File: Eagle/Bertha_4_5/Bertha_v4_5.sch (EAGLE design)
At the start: 132 parts, among them CON1 JACK_DC_BARREL, CON2 JACK_DC_BARREL, IC1 MCP1703DB, IC4 DRV8811, J1 RJ12RIGHTANGLE-I2C, J2 RJ12RIGHTANGLE-I2C, Q5 BSP75, Q6 BSP75, U1 HX711, U100 RN2483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

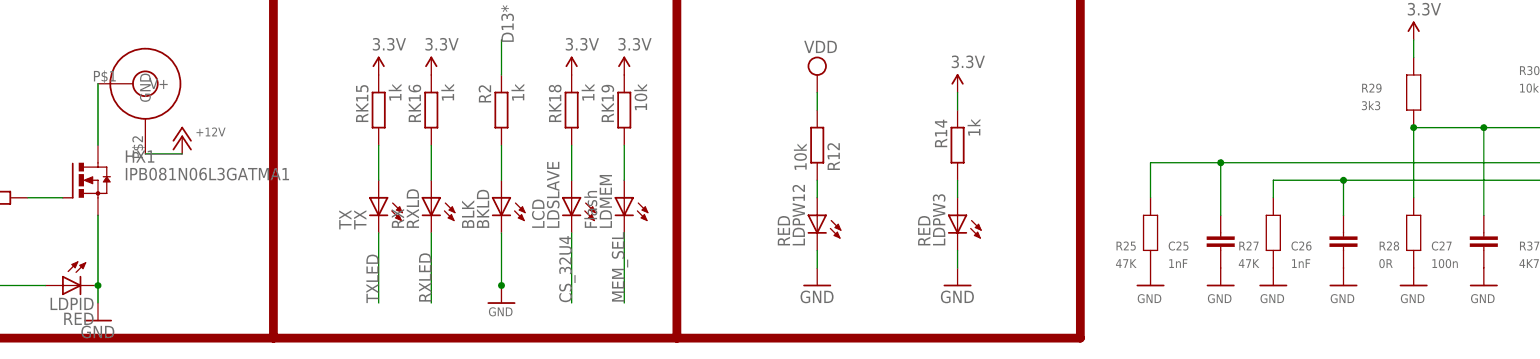
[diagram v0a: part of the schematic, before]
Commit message: correted PID diode, 4.5 finished, closes #72, ref #47
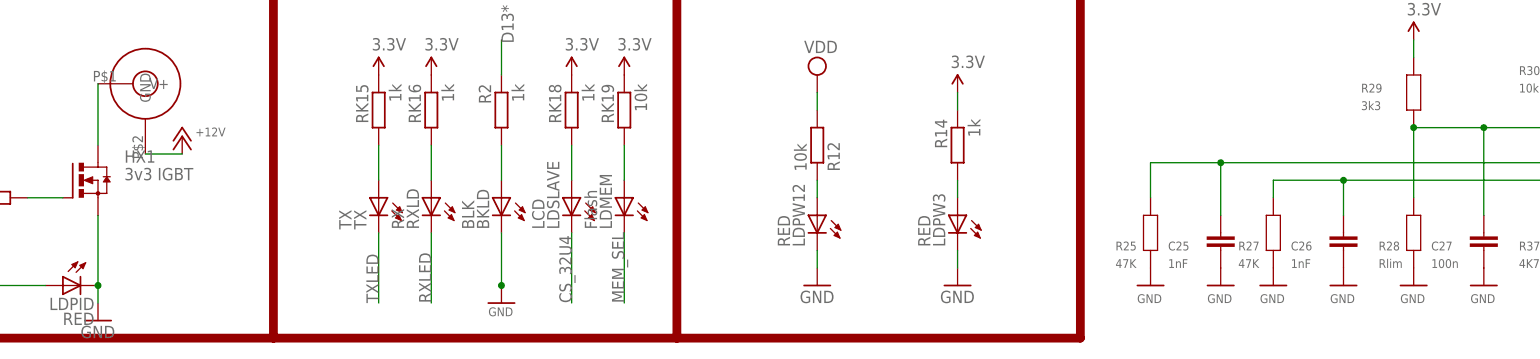
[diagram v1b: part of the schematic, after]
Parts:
- HX1: value IPB081N06L3GATMA1 -> 3v3 IGBT
- R28: value 0R -> Rlim
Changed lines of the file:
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@@
 <?xml version="1.0" encoding="utf-8"?>
 <!DOCTYPE eagle SYSTEM "eagle.dtd">
-<eagle version="7.7.0">
+<eagle version="6.5.0">
 <drawing>
 <settings>
@@
 <part name="GND8" library="supply1" deviceset="GND" device=""/>
 <part name="GND27" library="supply1" deviceset="GND" device=""/>
-<part name="HX1" library="transistor-power" deviceset="IRF3704" device="S" value="IPB081N06L3GATMA1"/>
+<part name="HX1" library="transistor-power" deviceset="IRF3704" device="S" value="3v3 IGBT"/>
 <part name="R11" library="rcl" deviceset="R-EU_" device="R0805" value="1K"/>
 <part name="P+2" library="supply1" deviceset="+12V" device=""/>
@@
 <part name="R27" library="freetronics-master-v1" deviceset="RESISTOR" device="0805" value="47K"/>
 <part name="C26" library="freetronics-master-v1" deviceset="CAP" device="0805" value="1nF"/>
-<part name="R28" library="freetronics-master-v1" deviceset="RESISTOR" device="0805" value="0R"/>
+<part name="R28" library="freetronics-master-v1" deviceset="RESISTOR" device="0805" value="Rlim"/>
 <part name="C27" library="freetronics-master-v1" deviceset="CAP" device="0805" value="100n"/>
 <part name="R29" library="freetronics-master-v1" deviceset="RESISTOR" device="0805" value="3k3"/>

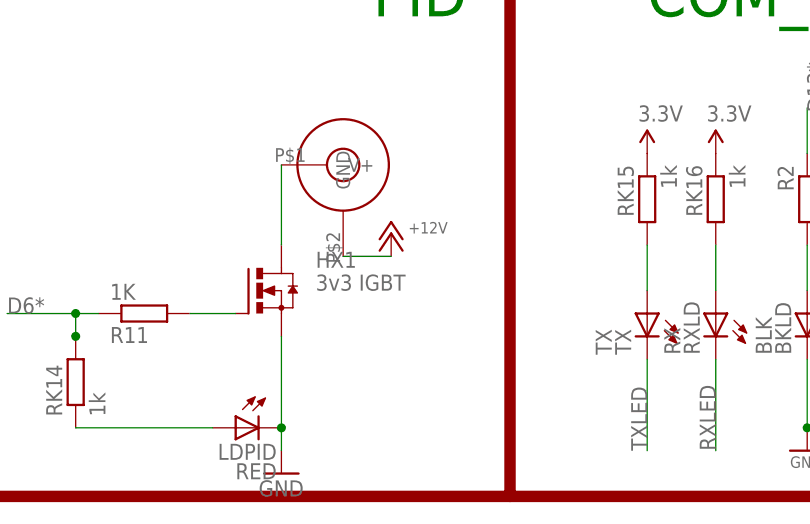
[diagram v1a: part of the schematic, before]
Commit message: corrected powerFET labelling
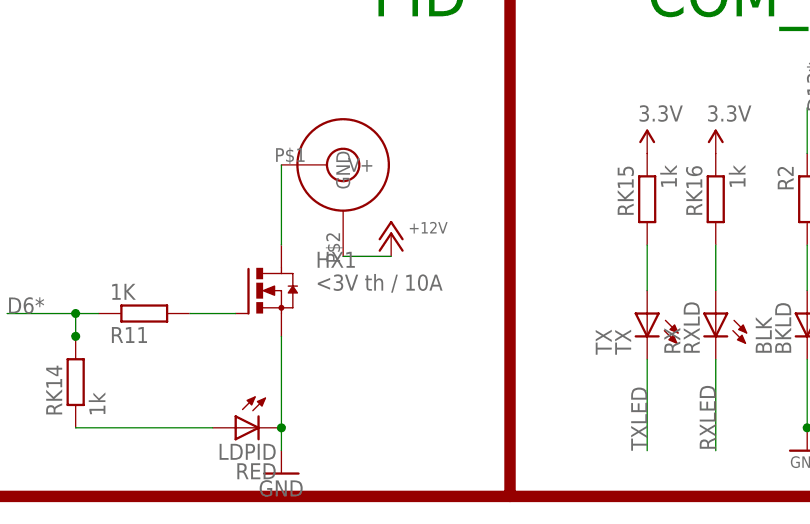
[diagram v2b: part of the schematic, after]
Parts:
- HX1: value 3v3 IGBT -> <3V th / 10A
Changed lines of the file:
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@@
 <part name="GND8" library="supply1" deviceset="GND" device=""/>
 <part name="GND27" library="supply1" deviceset="GND" device=""/>
-<part name="HX1" library="transistor-power" deviceset="IRF3704" device="S" value="3v3 IGBT"/>
+<part name="HX1" library="transistor-power" deviceset="IRF3704" device="S" value="&lt;3V th / 10A"/>
 <part name="R11" library="rcl" deviceset="R-EU_" device="R0805" value="1K"/>
 <part name="P+2" library="supply1" deviceset="+12V" device=""/>

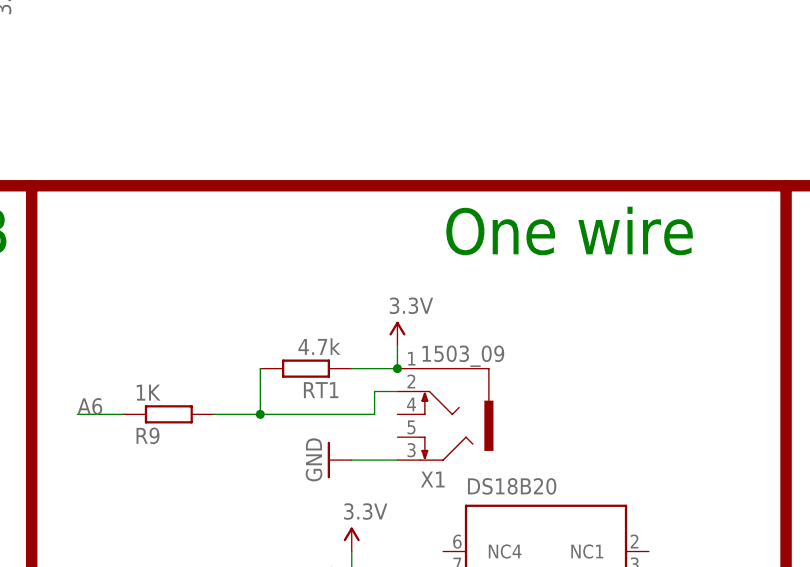
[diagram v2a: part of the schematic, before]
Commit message: added protection resistor, closes #74
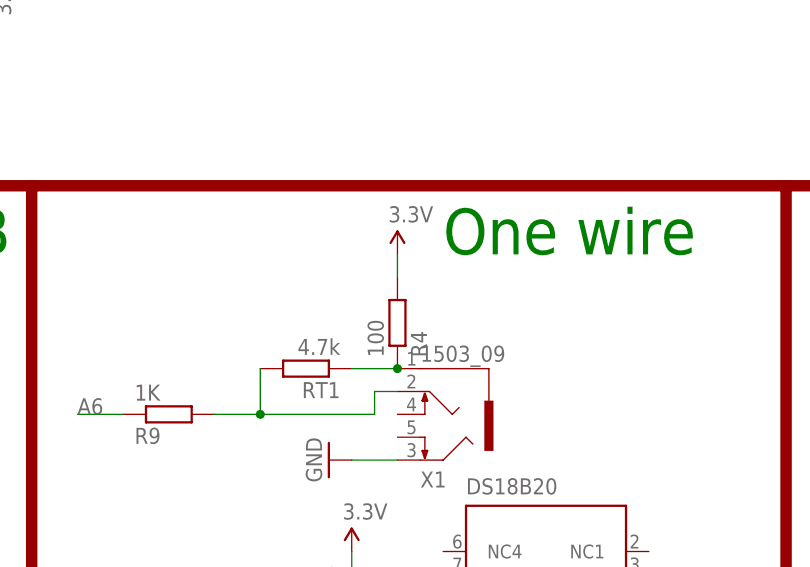
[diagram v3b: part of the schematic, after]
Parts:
- added R4: 100, rcl:R-EU_R0805
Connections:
- new net N$14: R4.1, RT1.1, X1.1
- net 3.3V: now also R4.2; no longer RT1.1, X1.1
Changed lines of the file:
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@@
 <part name="P+62" library="SparkFun" deviceset="3.3V" device=""/>
 <part name="JP3" library="jumper" deviceset="JP4E" device=""/>
+<part name="R4" library="rcl" deviceset="R-EU_" device="R0805" value="100"/>
 </parts>
 <sheets>
@@
 <instance part="P+35" gate="G$1" x="30.48" y="116.84"/>
 <instance part="P+36" gate="G$1" x="274.32" y="27.94"/>
-<instance part="P+37" gate="G$1" x="279.4" y="50.8"/>
+<instance part="P+37" gate="G$1" x="279.4" y="60.96"/>
 <instance part="P+39" gate="G$1" x="401.32" y="45.72"/>
 <instance part="P+40" gate="G$1" x="408.94" y="45.72"/>
@@
 <instance part="P+62" gate="G$1" x="693.42" y="53.34"/>
 <instance part="JP3" gate="G$1" x="673.1" y="48.26" rot="R270"/>
+<instance part="R4" gate="G$1" x="279.4" y="53.34" rot="MR90"/>
 </instances>
 <busses>
@@
 </segment>
 <segment>
-<pinref part="RT1" gate="G$1" pin="1"/>
-<pinref part="P+37" gate="G$1" pin="3.3V"/>
-<wire x1="279.4" y1="50.8" x2="279.4" y2="48.26" width="0.1524" layer="91"/>
-<pinref part="X1" gate="G$1" pin="1"/>
-<junction x="279.4" y="48.26"/>
-<wire x1="279.4" y1="48.26" x2="274.32" y2="48.26" width="0.1524" layer="91"/>
-</segment>
-<segment>
 <pinref part="RK15" gate="G$1" pin="1"/>
 <pinref part="P+39" gate="G$1" pin="3.3V"/>
@@
 <pinref part="P+62" gate="G$1" pin="3.3V"/>
 </segment>
+<segment>
+<pinref part="R4" gate="G$1" pin="2"/>
+<pinref part="P+37" gate="G$1" pin="3.3V"/>
+<wire x1="279.4" y1="60.96" x2="279.4" y2="58.42" width="0.1524" layer="91"/>
+</segment>
 </net>
 <net name="SDA" class="0">
@@
 </segment>
 </net>
+<net name="N$14" class="1">
+<segment>
+<pinref part="RT1" gate="G$1" pin="1"/>
+<pinref part="X1" gate="G$1" pin="1"/>
+<wire x1="279.4" y1="48.26" x2="274.32" y2="48.26" width="0.1524" layer="91"/>
+<pinref part="R4" gate="G$1" pin="1"/>
+<junction x="279.4" y="48.26"/>
+</segment>
+</net>

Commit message: added high side power switch with 5.6V zener on V4.5, drafted hack modif on 4.4, To be tested
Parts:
- added BJ2: MMBT4403, SparkFun-DiscreteSemi:TRANSISTOR_PNPMMBT4403
- added D6: 5.6V ZNR, diode:ZENER-DIODESOD80C
- added RK17, RK20: 1k, rcl:R-EU_R0805
- added T1: 2n7002, zetex:NMOSSOT23
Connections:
- new net N$16: BJ2.C, R11.1, RK14.2
- new net N$19: BJ2.E, D6.C, RK17.1
- new net N$31: BJ2.B, RK20.1
- new net N$32: RK20.2, T1.D
- net +12V: now also RK17.2
- net D6*: now also T1.G; no longer R11.1, RK14.2
- net GND: now also D6.A, T1.S
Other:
- moved on the sheet: CU7, CU8, IC1

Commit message: pretty sch for 4.5
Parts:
- RK14: value 1k -> 10k
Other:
- moved on the sheet: 12V, 32U4, 3V3, C10, C11, C12, C13, C25, C26, C27, C28, C29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

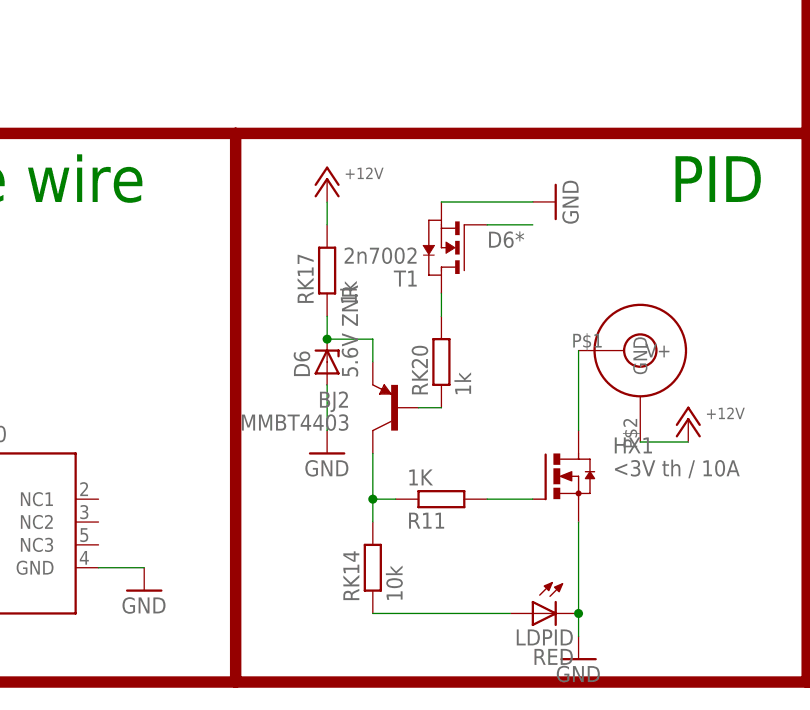
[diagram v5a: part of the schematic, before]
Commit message: JTAG on top
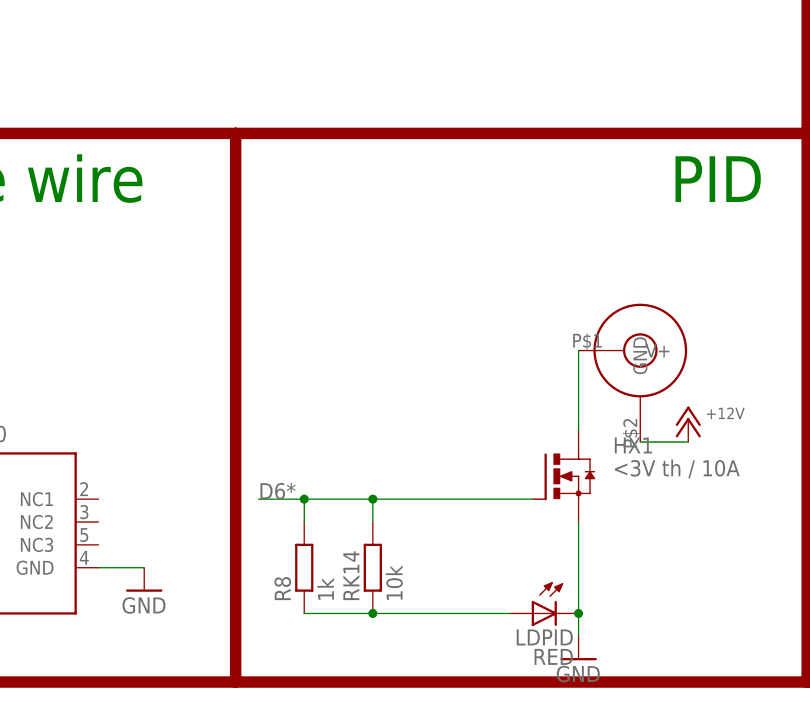
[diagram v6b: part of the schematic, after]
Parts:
- removed BJ2: MMBT4403, SparkFun-DiscreteSemi:TRANSISTOR_PNPMMBT4403
- removed D6: 5.6V ZNR, diode:ZENER-DIODESOD80C
- removed R11: 1K, rcl:R-EU_R0805
- removed RK17, RK20: 1k, rcl:R-EU_R0805
- removed T1: 2n7002, zetex:NMOSSOT23
- added R8: 1k, rcl:R-EU_R0805
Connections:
- removed net N$16: BJ2.C, R11.1, RK14.2
- removed net N$19: BJ2.E, D6.C, RK17.1
- removed net N$31: BJ2.B, RK20.1
- removed net N$32: RK20.2, T1.D
- removed net N$6: HX1.G, R11.2
- net +12V: no longer RK17.2
- net D6*: now also HX1.G, R8.2, RK14.2; no longer T1.G
- net GND: no longer D6.A, T1.S
- net N$26: now also R8.1
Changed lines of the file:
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@@
 <?xml version="1.0" encoding="utf-8"?>
 <!DOCTYPE eagle SYSTEM "eagle.dtd">
-<eagle version="6.5.0">
+<eagle version="8.0.1">
 <drawing>
 <settings>
@@
 <part name="GND27" library="supply1" deviceset="GND" device=""/>
 <part name="HX1" library="transistor-power" deviceset="IRF3704" device="S" value="&lt;3V th / 10A"/>
-<part name="R11" library="rcl" deviceset="R-EU_" device="R0805" value="1K"/>
 <part name="P+2" library="supply1" deviceset="+12V" device=""/>
 <part name="GND2" library="supply1" deviceset="GND" device=""/>
@@
 <part name="JP3" library="jumper" deviceset="JP4E" device=""/>
 <part name="R4" library="rcl" deviceset="R-EU_" device="R0805" value="100"/>
-<part name="P+13" library="supply1" deviceset="+12V" device=""/>
-<part name="BJ2" library="SparkFun-DiscreteSemi" deviceset="TRANSISTOR_PNP" device="MMBT4403" value="MMBT4403"/>
-<part name="GND5" library="supply1" deviceset="GND" device=""/>
-<part name="RK17" library="rcl" deviceset="R-EU_" device="R0805" value="1k"/>
-<part name="T1" library="zetex" deviceset="NMOSSOT23" device="" value="2n7002"/>
-<part name="RK20" library="rcl" deviceset="R-EU_" device="R0805" value="1k"/>
-<part name="GND9" library="supply1" deviceset="GND" device=""/>
-<part name="D6" library="diode" deviceset="ZENER-DIODE" device="SOD80C" value="5.6V ZNR"/>
+<part name="R8" library="rcl" deviceset="R-EU_" device="R0805" value="1k"/>
 </parts>
 <sheets>
@@
 <instance part="GND27" gate="1" x="337.82" y="266.7"/>
 <instance part="HX1" gate="G$1" x="358.14" y="30.48"/>
-<instance part="R11" gate="G$1" x="345.44" y="27.94" rot="MR180"/>
 <instance part="P+2" gate="1" x="372.872" y="36.83" smashed="yes">
 <attribute name="VALUE" x="374.777" y="36.83" size="1.27" layer="96"/>
@@
 <instance part="JP3" gate="G$1" x="350.52" y="127" rot="R270"/>
 <instance part="R4" gate="G$1" x="279.4" y="53.34" rot="MR90"/>
-<instance part="P+13" gate="1" x="332.74" y="63.5" smashed="yes">
-<attribute name="VALUE" x="334.645" y="63.5" size="1.27" layer="96"/>
-</instance>
-<instance part="BJ2" gate="G$1" x="340.36" y="38.1" rot="MR0"/>
-<instance part="GND5" gate="1" x="332.74" y="33.02"/>
-<instance part="RK17" gate="G$1" x="332.74" y="53.34" rot="R90"/>
-<instance part="T1" gate="A" x="345.44" y="55.88" rot="R180"/>
-<instance part="RK20" gate="G$1" x="345.44" y="43.18" rot="R90"/>
-<instance part="GND9" gate="1" x="358.14" y="60.96" rot="R90"/>
-<instance part="D6" gate="G$1" x="332.74" y="43.18" rot="R90"/>
+<instance part="R8" gate="G$1" x="330.2" y="20.32" rot="R90"/>
 </instances>
 <busses>
@@
 <pinref part="U$38" gate="G$1" pin="GND"/>
 </segment>
-<segment>
-<pinref part="GND5" gate="1" pin="GND"/>
-<wire x1="332.74" y1="35.56" x2="332.74" y2="40.64" width="0.1524" layer="91"/>
-<pinref part="D6" gate="G$1" pin="A"/>
-</segment>
-<segment>
-<pinref part="T1" gate="A" pin="S"/>
-<pinref part="GND9" gate="1" pin="GND"/>
-<wire x1="355.6" y1="60.96" x2="345.44" y2="60.96" width="0.1524" layer="91"/>
-</segment>
 </net>
 <net name="SCK" class="0">
@@
 </segment>
 <segment>
-<pinref part="T1" gate="A" pin="G"/>
-<wire x1="350.52" y1="58.42" x2="355.6" y2="58.42" width="0.1524" layer="91"/>
-<label x="350.52" y="55.88" size="1.778" layer="95"/>
+<pinref part="HX1" gate="G$1" pin="G"/>
+<wire x1="325.12" y1="27.94" x2="330.2" y2="27.94" width="0.1524" layer="91"/>
+<wire x1="330.2" y1="27.94" x2="337.82" y2="27.94" width="0.1524" layer="91"/>
+<wire x1="337.82" y1="27.94" x2="337.82" y2="25.4" width="0.1524" layer="91"/>
+<junction x="337.82" y="27.94"/>
+<pinref part="RK14" gate="G$1" pin="2"/>
+<wire x1="355.6" y1="27.94" x2="337.82" y2="27.94" width="0.1524" layer="91"/>
+<label x="325.12" y="27.94" size="1.778" layer="95"/>
+<pinref part="R8" gate="G$1" pin="2"/>
+<wire x1="330.2" y1="25.4" x2="330.2" y2="27.94" width="0.1524" layer="91"/>
+<junction x="330.2" y="27.94"/>
 </segment>
 </net>
@@
 <pinref part="C47" gate="G$1" pin="+"/>
 </segment>
-<segment>
-<pinref part="P+13" gate="1" pin="+12V"/>
-<pinref part="RK17" gate="G$1" pin="2"/>
-<wire x1="332.74" y1="60.96" x2="332.74" y2="58.42" width="0.1524" layer="91"/>
-</segment>
 </net>
 <net name="3.3V" class="1">
@@
 </segment>
 </net>
-<net name="N$6" class="0">
-<segment>
-<pinref part="R11" gate="G$1" pin="2"/>
-<pinref part="HX1" gate="G$1" pin="G"/>
-<wire x1="350.52" y1="27.94" x2="355.6" y2="27.94" width="0.1524" layer="91"/>
-</segment>
-</net>
 <net name="N$3" class="0">
 <segment>
@@
 <wire x1="353.06" y1="15.24" x2="337.82" y2="15.24" width="0.1524" layer="91"/>
 <pinref part="LDPID" gate="G$1" pin="A"/>
+<pinref part="R8" gate="G$1" pin="1"/>
+<wire x1="330.2" y1="15.24" x2="337.82" y2="15.24" width="0.1524" layer="91"/>
+<junction x="337.82" y="15.24"/>
 </segment>
 </net>
@@
 </segment>
 </net>
-<net name="N$16" class="0">
-<segment>
-<pinref part="BJ2" gate="G$1" pin="C"/>
-<wire x1="337.82" y1="33.02" x2="337.82" y2="27.94" width="0.1524" layer="91"/>
-<pinref part="R11" gate="G$1" pin="1"/>
-<wire x1="337.82" y1="27.94" x2="337.82" y2="25.4" width="0.1524" layer="91"/>
-<wire x1="340.36" y1="27.94" x2="337.82" y2="27.94" width="0.1524" layer="91"/>
-<junction x="337.82" y="27.94"/>
-<pinref part="RK14" gate="G$1" pin="2"/>
-</segment>
-</net>
-<net name="N$19" class="0">
-<segment>
-<pinref part="RK17" gate="G$1" pin="1"/>
-<wire x1="332.74" y1="45.72" x2="332.74" y2="48.26" width="0.1524" layer="91"/>
-<wire x1="332.74" y1="45.72" x2="337.82" y2="45.72" width="0.1524" layer="91"/>
-<pinref part="BJ2" gate="G$1" pin="E"/>
-<wire x1="337.82" y1="45.72" x2="337.82" y2="43.18" width="0.1524" layer="91"/>
-<pinref part="D6" gate="G$1" pin="C"/>
-<junction x="332.74" y="45.72"/>
-</segment>
-</net>
-<net name="N$31" class="0">
-<segment>
-<pinref part="BJ2" gate="G$1" pin="B"/>
-<wire x1="342.9" y1="38.1" x2="345.44" y2="38.1" width="0.1524" layer="91"/>
-<pinref part="RK20" gate="G$1" pin="1"/>
-</segment>
-</net>
-<net name="N$32" class="0">
-<segment>
-<pinref part="RK20" gate="G$1" pin="2"/>
-<pinref part="T1" gate="A" pin="D"/>
-<wire x1="345.44" y1="48.26" x2="345.44" y2="50.8" width="0.1524" layer="91"/>
-</segment>
-</net>

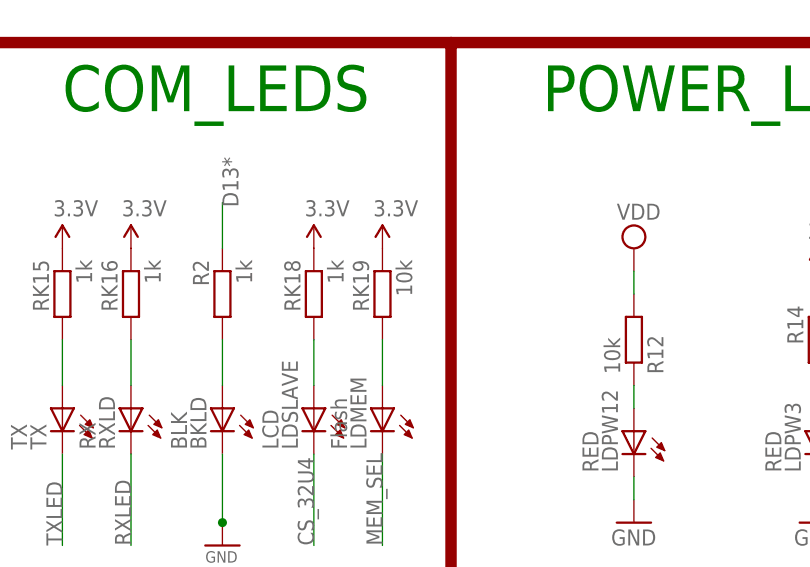
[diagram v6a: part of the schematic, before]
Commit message: change resistor select flash to 1k
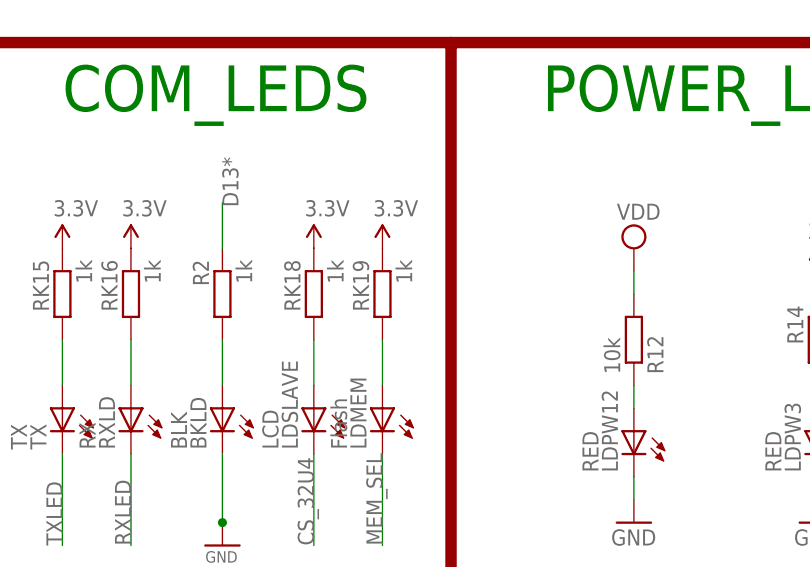
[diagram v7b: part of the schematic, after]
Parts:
- RK19: value 10k -> 1k
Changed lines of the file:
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@@
 <?xml version="1.0" encoding="utf-8"?>
 <!DOCTYPE eagle SYSTEM "eagle.dtd">
-<eagle version="8.0.1">
+<eagle version="7.7.0">
 <drawing>
 <settings>
@@
 <part name="RK16" library="rcl" deviceset="R-EU_" device="R0805" value="1k"/>
 <part name="RXLD" library="adafruit" deviceset="LED" device="CHIP-LED0805" value="RX"/>
-<part name="RK19" library="rcl" deviceset="R-EU_" device="R0805" value="10k"/>
+<part name="RK19" library="rcl" deviceset="R-EU_" device="R0805" value="1k"/>
 <part name="LDMEM" library="adafruit" deviceset="LED" device="CHIP-LED0805" value="Flash"/>
 <part name="C5" library="rcl" deviceset="C-EU" device="C0805" value="100n"/>
